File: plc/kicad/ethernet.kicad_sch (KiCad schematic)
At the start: 36 parts, among them U20 W5500, X1 X322525MRB4SI

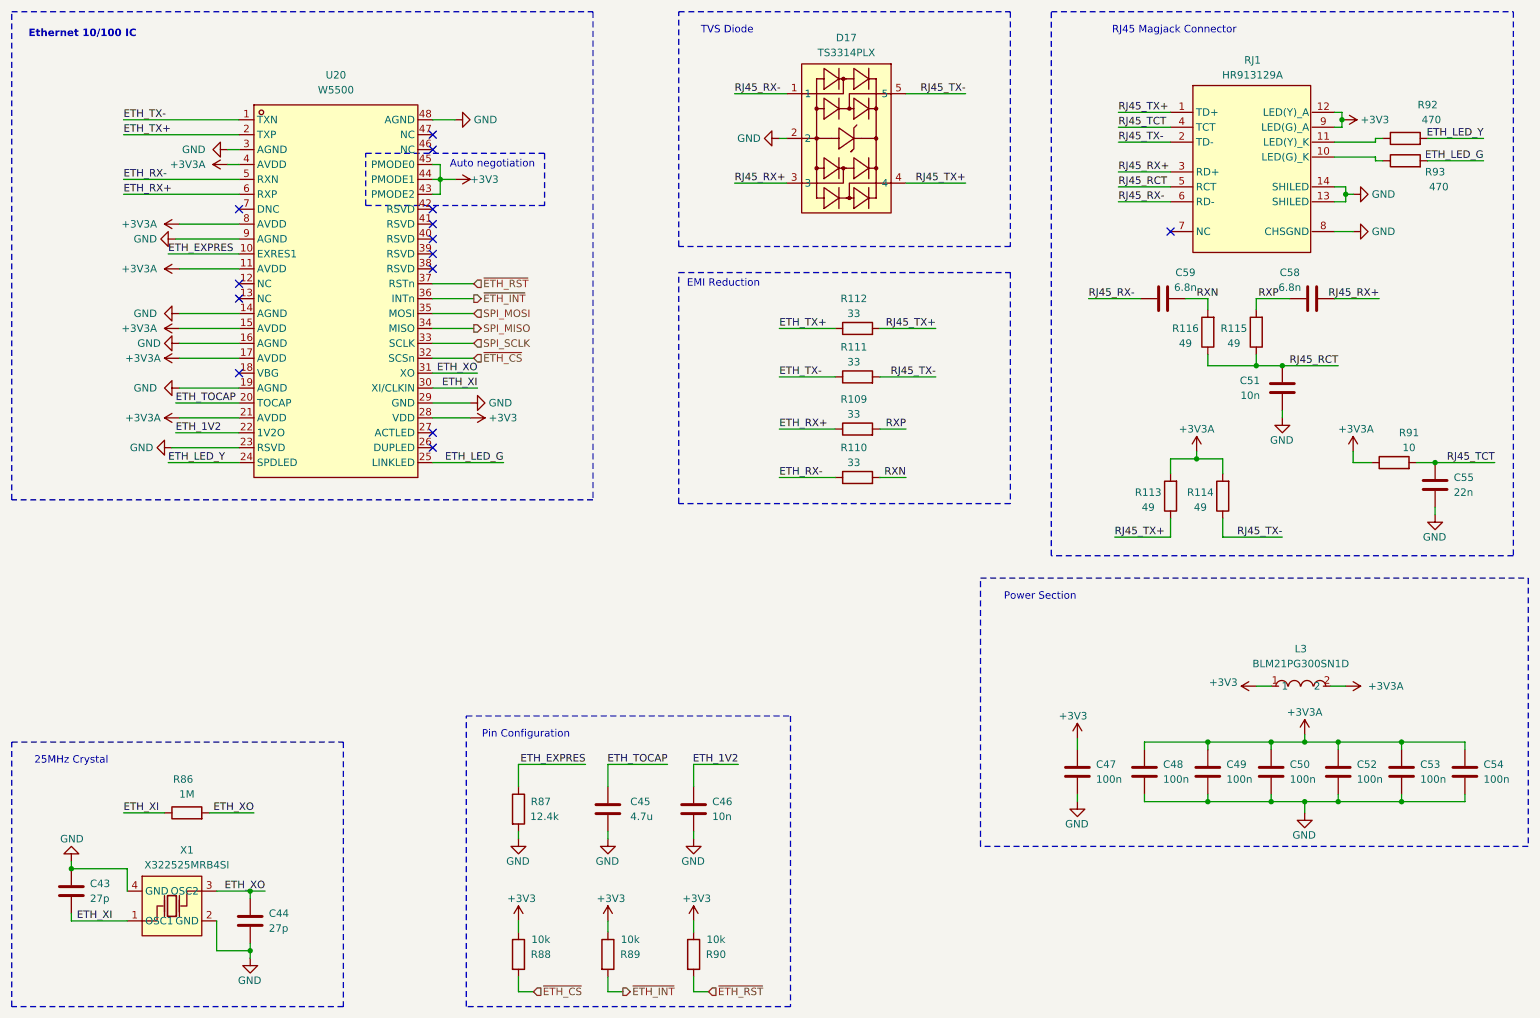
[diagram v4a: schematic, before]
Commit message: Rearranged small PCB placements
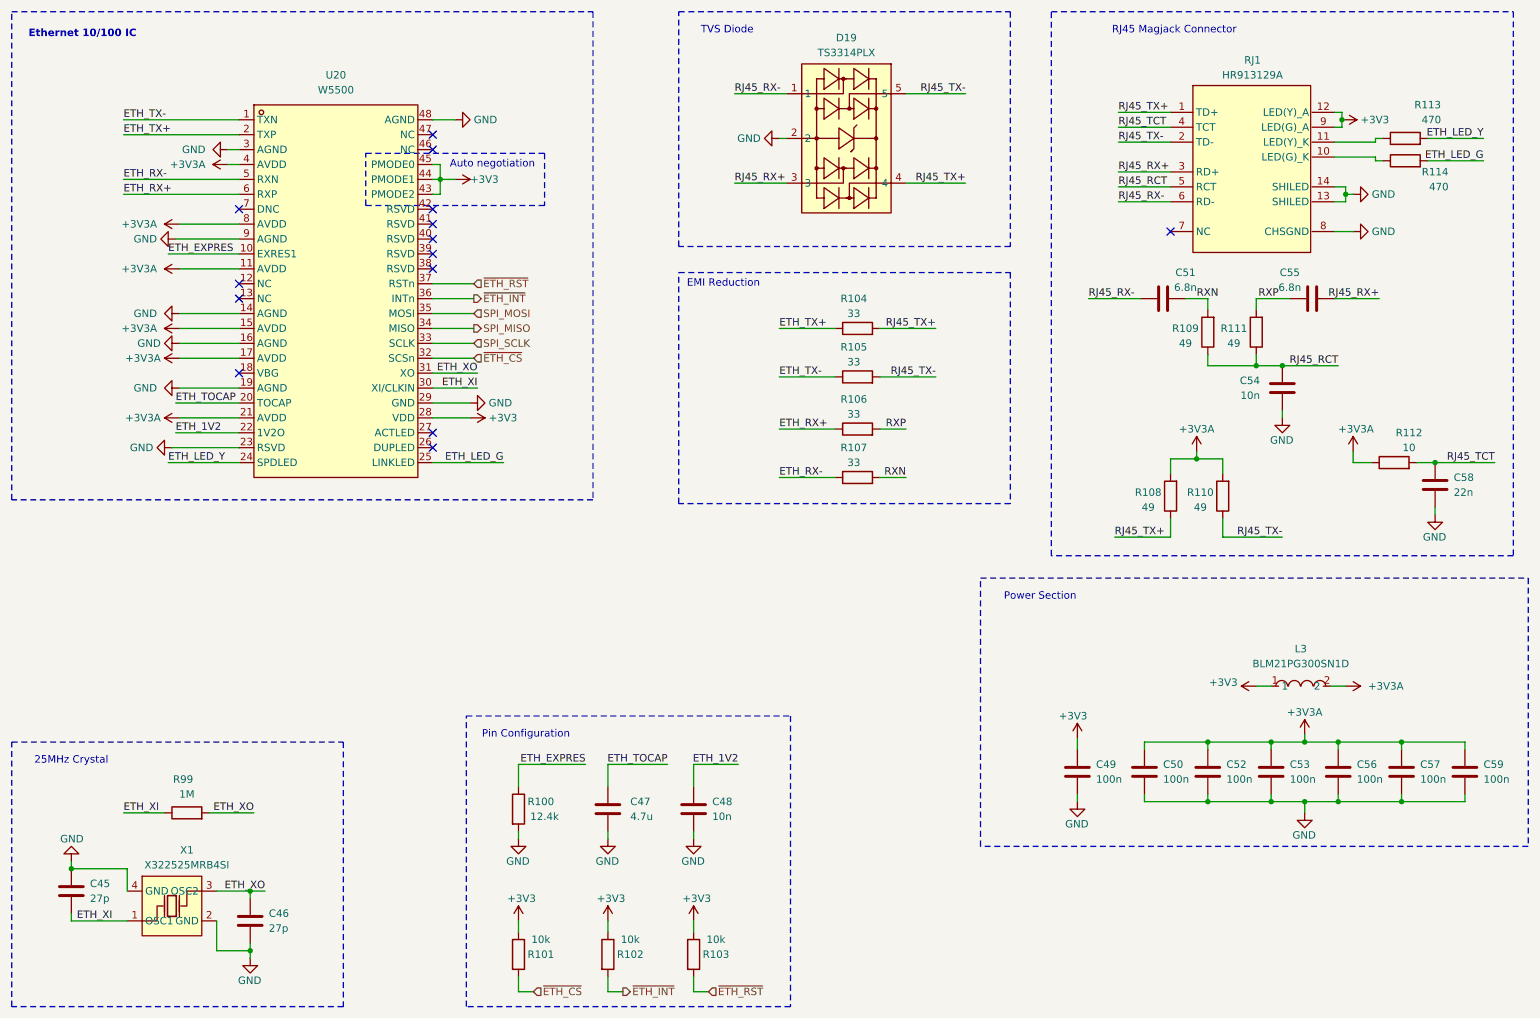
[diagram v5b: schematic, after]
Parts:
- renumbered C43 to C45, C44 to C46, C45 to C47, C46 to C48, C47 to C49, C48 to C50, C59 to C51, C49 to C52, C50 to C53, C51 to C54, C58 to C55, C52 to C56, C53 to C57, C55 to C58, C54 to C59, D17 to D19, R87 to R100, R88 to R101, R89 to R102, R90 to R103, R112 to R104, R111 to R105, R109 to R106, R110 to R107, R113 to R108, R116 to R109, R114 to R110, R115 to R111, R91 to R112, R92 to R113, R93 to R114, R86 to R99

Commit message: Routed Ethernet at 100 ohms
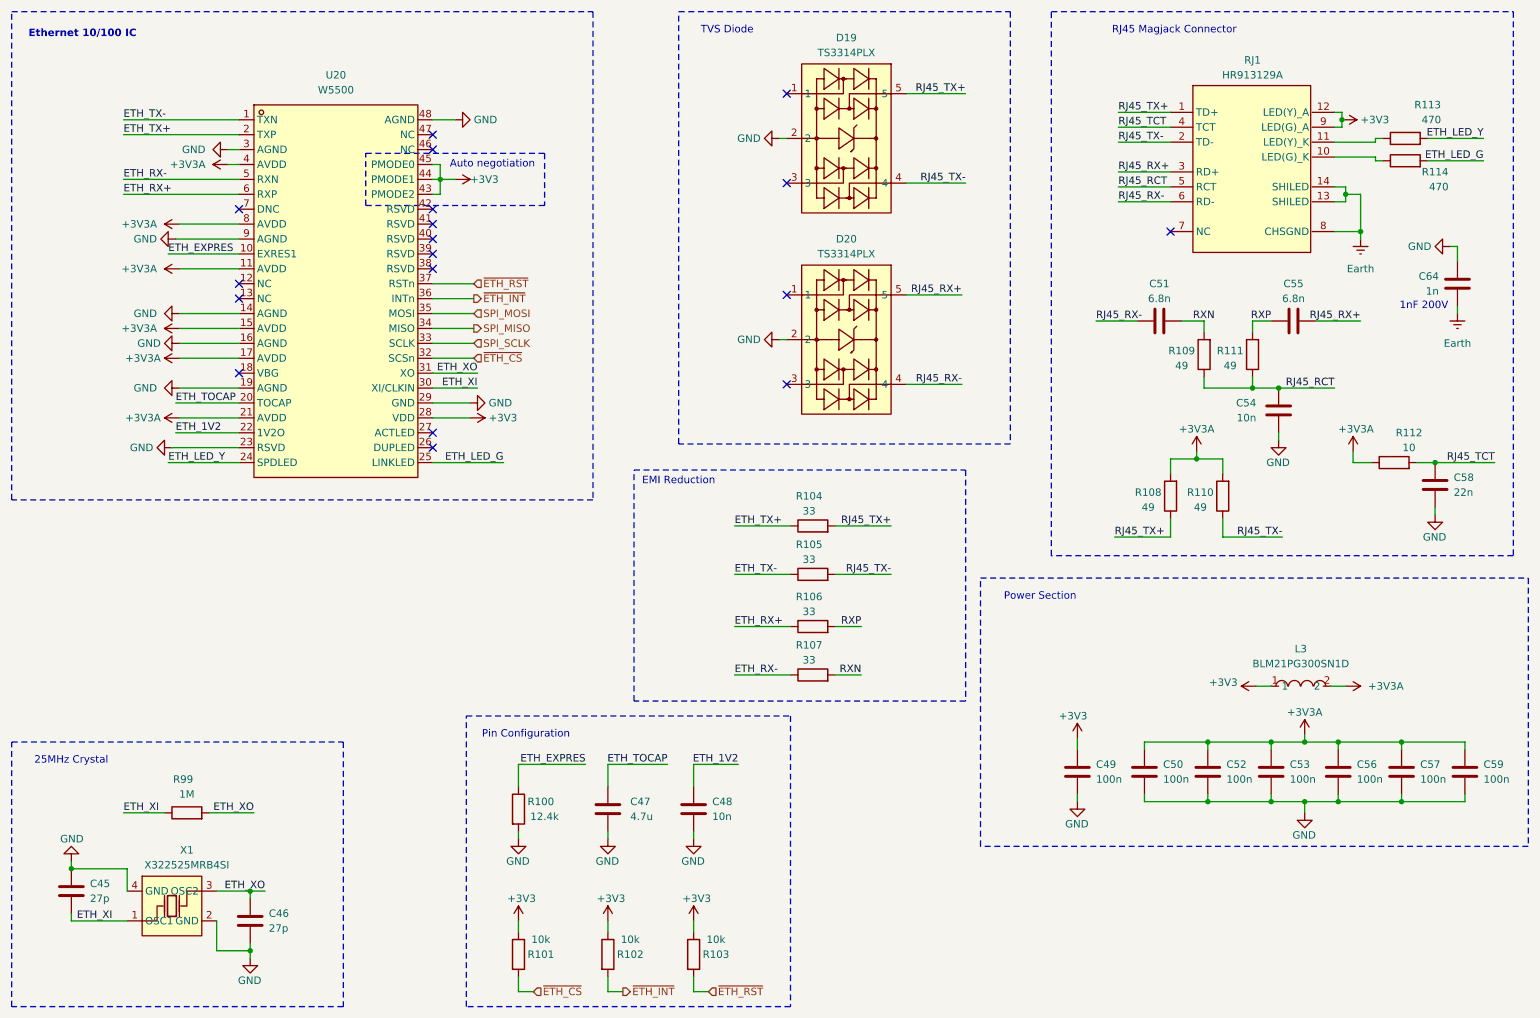
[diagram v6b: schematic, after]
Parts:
- added C64: 1n, Capacitor_SMD:C_0603_1608Metric, symbol Device:C
- added D20: TS3314PLX, LibrePLC32:SOT-23-5_L2.9-W1.6-P0.95-LS2.8-BR, symbol LibrePLC32:TS3314PLX
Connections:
- net GND: now also C64.1, D20.2; no longer RJ1.13 (SHILED), RJ1.14 (SHILED), RJ1.8 (CHSGND)
- net RJ45_RX+: now also D20.5; no longer D19.3
- net RJ45_RX-: now also D20.4; no longer D19.1
- net RJ45_TX+: now also D19.5; no longer D19.4
- net RJ45_TX-: now also D19.4; no longer D19.5
- new net Earth: C64.2, RJ1.13 (SHILED), RJ1.14 (SHILED), RJ1.8 (CHSGND)
- no-connect marks 14 -> 18
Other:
- note added: "1nF 200V"
- moved on the sheet: C51, C54, C55, R104, R105, R106, R107, R109, R111

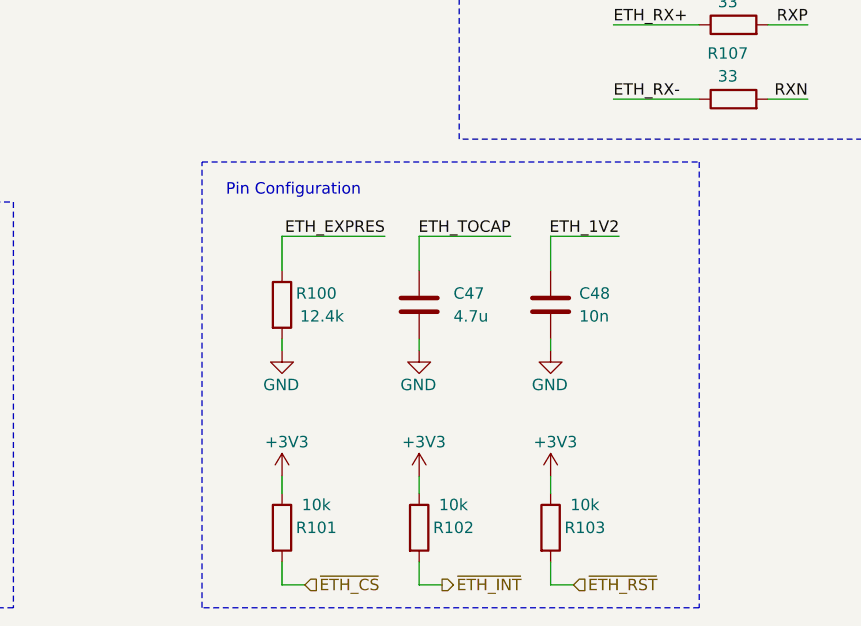
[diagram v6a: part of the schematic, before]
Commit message: BOM Consolidation
- CP2102N Vdbg divider: 22.1k→5.1k, 47.5k→10k (gives 3.29V)
- I²C pull-ups (R65,R66): 4.7k→5.1k (verified ok)
- Buck UVLO (R69,R70): 442k→100k, 90.9k→2×10k (UVLO = 7V)
- TPS272C45D ILIM (R75): 3k→3×10k (~6A limit)
- PPIC IMON + ETH_EXPRESS (R77,R100): 12.4k→2×6.2k
- Buck compensation (R78): 16.9k→10k+6.2k+620 series
- PPIC PGTH divider (R79,R80): 499k→100k, 55.44k→2×10k (PGTH = 7.2V)
- Buck feedback (R82,R83): 53.6k→52.5k 1%, 10.2k→10k 1%
- 3.3V LDO power-good (R88): 50k→100k

| Metric                 | Before | After | Change             |
| ---------------------- | ------ | ----- | ------------------ |
| Unique resistor values | 33     | 22    | **−11 (−33%)**     |
| Total resistor count   | 110    | 118   | +8 (series splits) |
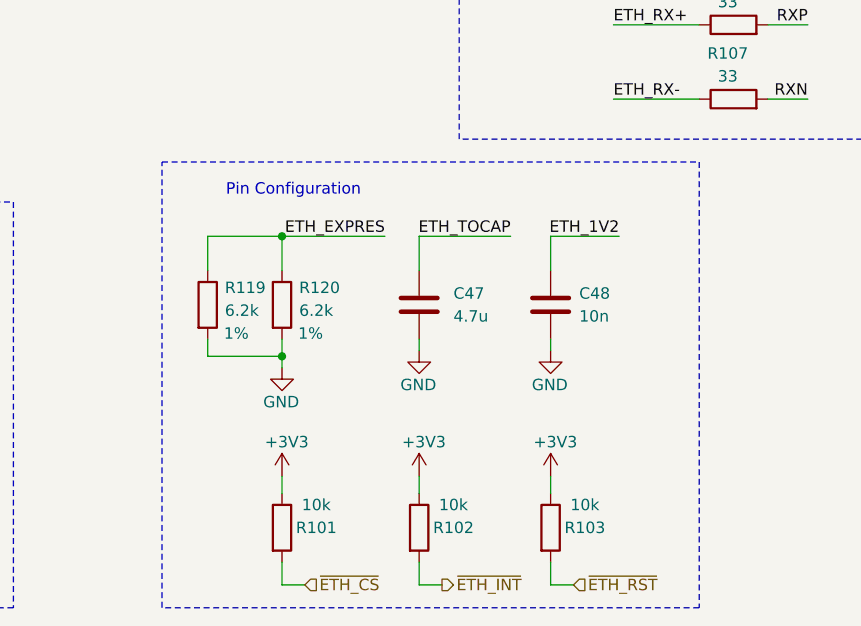
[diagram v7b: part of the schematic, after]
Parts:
- removed R100: 12.4k, Resistor_SMD:R_0603_1608Metric, symbol Device:R
- added R119, R120: 6.2k, Resistor_SMD:R_0603_1608Metric, symbol Device:R
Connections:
- net ETH_EXPRES: now also R119.1, R120.1
- net GND: now also R119.2, R120.2
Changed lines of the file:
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@@
 	)
 	(rectangle
-		(start 98.425 139.7)
+		(start 93.98 139.7)
 		(end 153.67 189.23)
 		(stroke
@@
 	)
 	(junction
+		(at 107.315 147.955)
+		(diameter 0)
+		(color 0 0 0 0)
+	)
+	(junction
 		(at 235.585 154.305)
 		(diameter 0)
@@
 	)
 	(junction
+		(at 107.315 161.29)
+		(diameter 0)
+		(color 0 0 0 0)
+	)
+	(junction
 		(at 31.115 165.735)
 		(diameter 0)
@@
 	(wire
 		(pts
+			(xy 107.315 161.29) (xy 107.315 162.56)
+		)
+		(stroke
+			(width 0)
+			(type default)
+		)
+	)
+	(wire
+		(pts
 			(xy 224.79 144.145) (xy 213.995 144.145)
 		)
@@
 	(wire
 		(pts
+			(xy 99.06 151.765) (xy 99.06 147.955)
+		)
+		(stroke
+			(width 0)
+			(type default)
+		)
+	)
+	(wire
+		(pts
 			(xy 241.3 154.305) (xy 247.015 154.305)
 		)
@@
 	(wire
 		(pts
+			(xy 107.315 161.29) (xy 99.06 161.29)
+		)
+		(stroke
+			(width 0)
+			(type default)
+		)
+	)
+	(wire
+		(pts
 			(xy 92.71 73.66) (xy 99.695 73.66)
 		)
@@
 	(wire
 		(pts
+			(xy 99.06 147.955) (xy 107.315 147.955)
+		)
+		(stroke
+			(width 0)
+			(type default)
+		)
+	)
+	(wire
+		(pts
 			(xy 209.55 46.99) (xy 218.44 46.99)
 		)
@@
 	(wire
 		(pts
-			(xy 107.315 159.385) (xy 107.315 160.655)
+			(xy 107.315 159.385) (xy 107.315 161.29)
 		)
 		(stroke
@@
 	(wire
 		(pts
+			(xy 99.06 161.29) (xy 99.06 159.385)
+		)
+		(stroke
+			(width 0)
+			(type default)
+		)
+	)
+	(wire
+		(pts
 			(xy 267.335 71.12) (xy 267.335 69.85)
 		)
@@
 	)
 	(symbol
+		(lib_id "Device:R")
+		(at 99.06 155.575 0)
+		(unit 1)
+		(body_style 1)
+		(exclude_from_sim no)
+		(in_bom yes)
+		(on_board yes)
+		(in_pos_files yes)
+		(dnp no)
+		(property "Reference" "R119"
+			(at 100.965 153.67 0)
+			(show_name no)
+			(do_not_autoplace no)
+			(effects
+				(font
+					(size 1.27 1.27)
+				)
+				(justify left)
+			)
+		)
+		(property "Value" "6.2k"
+			(at 100.965 156.21 0)
+			(show_name no)
+			(do_not_autoplace no)
+			(effects
+				(font
+					(size 1.27 1.27)
+				)
+				(justify left)
+			)
+		)
+		(property "Footprint" "Resistor_SMD:R_0603_1608Metric"
+			(at 97.282 155.575 90)
+			(hide yes)
+			(show_name no)
+			(do_not_autoplace no)
+			(effects
+				(font
+					(size 1.27 1.27)
+				)
+			)
+		)
+		(property "Datasheet" ""
+			(at 99.06 155.575 0)
+			(hide yes)
+			(show_name no)
+			(do_not_autoplace no)
+			(effects
+				(font
+					(size 1.27 1.27)
+				)
+			)
+		)
+		(property "Description" "Resistor"
+			(at 99.06 155.575 0)
+			(hide yes)
+			(show_name no)
+			(do_not_autoplace no)
+			(effects
+				(font
+					(size 1.27 1.27)
+				)
+			)
+		)
+		(property "Tolerance" "1%"
+			(at 102.235 158.75 0)
+			(show_name no)
+			(do_not_autoplace no)
+			(effects
+				(font
+					(size 1.27 1.27)
+				)
+			)
+		)
+		(pin "2"
+		)
+		(pin "1"
+		)
+		(instances
+			(project "LibrePLC32"
+				(path "/ef4c1a27-85a3-413a-9f93-a41c4f97eee5/b26cf163-b355-429e-a9f6-9813c59c646b"
+					(reference "R119")
+					(unit 1)
+				)
+			)
+		)
+	)
+	(symbol
 		(lib_id "power:GND")
 		(at 49.53 76.2 270)
@@
 	)
 	(symbol
+		(lib_id "Device:R")
+		(at 107.315 155.575 0)
+		(unit 1)
+		(body_style 1)
+		(exclude_from_sim no)
+		(in_bom yes)
+		(on_board yes)
+		(in_pos_files yes)
+		(dnp no)
+		(property "Reference" "R120"
+			(at 109.22 153.67 0)
+			(show_name no)
+			(do_not_autoplace no)
+			(effects
+				(font
+					(size 1.27 1.27)
+				)
+				(justify left)
+			)
+		)
+		(property "Value" "6.2k"
+			(at 109.22 156.21 0)
+			(show_name no)
+			(do_not_autoplace no)
+			(effects
+				(font
+					(size 1.27 1.27)
+				)
+				(justify left)
+			)
+		)
+		(property "Footprint" "Resistor_SMD:R_0603_1608Metric"
+			(at 105.537 155.575 90)
+			(hide yes)
+			(show_name no)
+			(do_not_autoplace no)
+			(effects
+				(font
+					(size 1.27 1.27)
+				)
+			)
+		)
+		(property "Datasheet" ""
+			(at 107.315 155.575 0)
+			(hide yes)
+			(show_name no)
+			(do_not_autoplace no)
+			(effects
+				(font
+					(size 1.27 1.27)
+				)
+			)
+		)
+		(property "Description" "Resistor"
+			(at 107.315 155.575 0)
+			(hide yes)
+			(show_name no)
+			(do_not_autoplace no)
+			(effects
+				(font
+					(size 1.27 1.27)
+				)
+			)
+		)
+		(property "Tolerance" "1%"
+			(at 110.49 158.75 0)
+			(show_name no)
+			(do_not_autoplace no)
+			(effects
+				(font
+					(size 1.27 1.27)
+				)
+			)
+		)
+		(pin "2"
+		)
+		(pin "1"
+		)
+		(instances
+			(project "LibrePLC32"
+				(path "/ef4c1a27-85a3-413a-9f93-a41c4f97eee5/b26cf163-b355-429e-a9f6-9813c59c646b"
+					(reference "R120")
+					(unit 1)
+				)
+			)
+		)
+	)
+	(symbol
 		(lib_id "power:GND")
 		(at 241.3 156.21 0)
@@
 	(symbol
 		(lib_id "power:GND")
-		(at 107.315 160.655 0)
+		(at 107.315 162.56 0)
 		(unit 1)
 		(body_style 1)
@@
 		(dnp no)
 		(property "Reference" "#PWR0241"
-			(at 107.315 167.005 0)
+			(at 107.315 168.91 0)
 			(hide yes)
 			(show_name no)
@@
 		)
 		(property "Value" "GND"
-			(at 109.22 164.465 0)
+			(at 109.22 166.37 0)
 			(show_name no)
 			(do_not_autoplace no)
@@
 		)
 		(property "Footprint" ""
-			(at 107.315 160.655 0)
+			(at 107.315 162.56 0)
 			(hide yes)
 			(show_name no)
@@
 		)
 		(property "Datasheet" ""
-			(at 107.315 160.655 0)
+			(at 107.315 162.56 0)
 			(hide yes)
 			(show_name no)
@@
 		)
 		(property "Description" "Power symbol creates a global label with name \"GND\" , ground"
-			(at 107.315 160.655 0)
+			(at 107.315 162.56 0)
 			(hide yes)
 			(show_name no)
@@
 					(unit 1)
 				)
-			)
-		)
-	)
-	(symbol
-		(lib_id "Device:R")
-		(at 107.315 155.575 0)
-		(unit 1)
-		(body_style 1)
-		(exclude_from_sim no)
-		(in_bom yes)
-		(on_board yes)
-		(in_pos_files yes)
-		(dnp no)
-		(property "Reference" "R100"
-			(at 111.125 154.305 0)
-			(show_name no)
-			(do_not_autoplace no)
-			(effects
-				(font
-					(size 1.27 1.27)
-				)
-			)
-		)
-		(property "Value" "12.4k"
-			(at 111.76 156.845 0)
-			(show_name no)
-			(do_not_autoplace no)
-			(effects
-				(font
-					(size 1.27 1.27)
-				)
-			)
-		)
-		(property "Footprint" "Resistor_SMD:R_0603_1608Metric"
-			(at 105.537 155.575 90)
-			(hide yes)
-			(show_name no)
-			(do_not_autoplace no)
-			(effects
-				(font
-					(size 1.27 1.27)
-				)
-			)
-		)
-		(property "Datasheet" ""
-			(at 107.315 155.575 0)
-			(hide yes)
-			(show_name no)
-			(do_not_autoplace no)
-			(effects
-				(font
-					(size 1.27 1.27)
-				)
-			)
-		)
-		(property "Description" "Resistor"
-			(at 107.315 155.575 0)
-			(hide yes)
-			(show_name no)
-			(do_not_autoplace no)
-			(effects
-				(font
-					(size 1.27 1.27)
-				)
-			)
-		)
-		(pin "2"
-		)
-		(pin "1"
-		)
-		(instances
-			(project "LibrePLC32"
-				(path "/ef4c1a27-85a3-413a-9f93-a41c4f97eee5/b26cf163-b355-429e-a9f6-9813c59c646b"
-					(reference "R100")
-					(unit 1)
-				)
